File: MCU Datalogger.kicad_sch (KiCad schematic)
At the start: 18 parts, among them U1 24LC1025, U2 24LC1025, U3 DS1337S_, U4 ATMEGA328P-AU, Y1 Crystal, Y2 Crystal

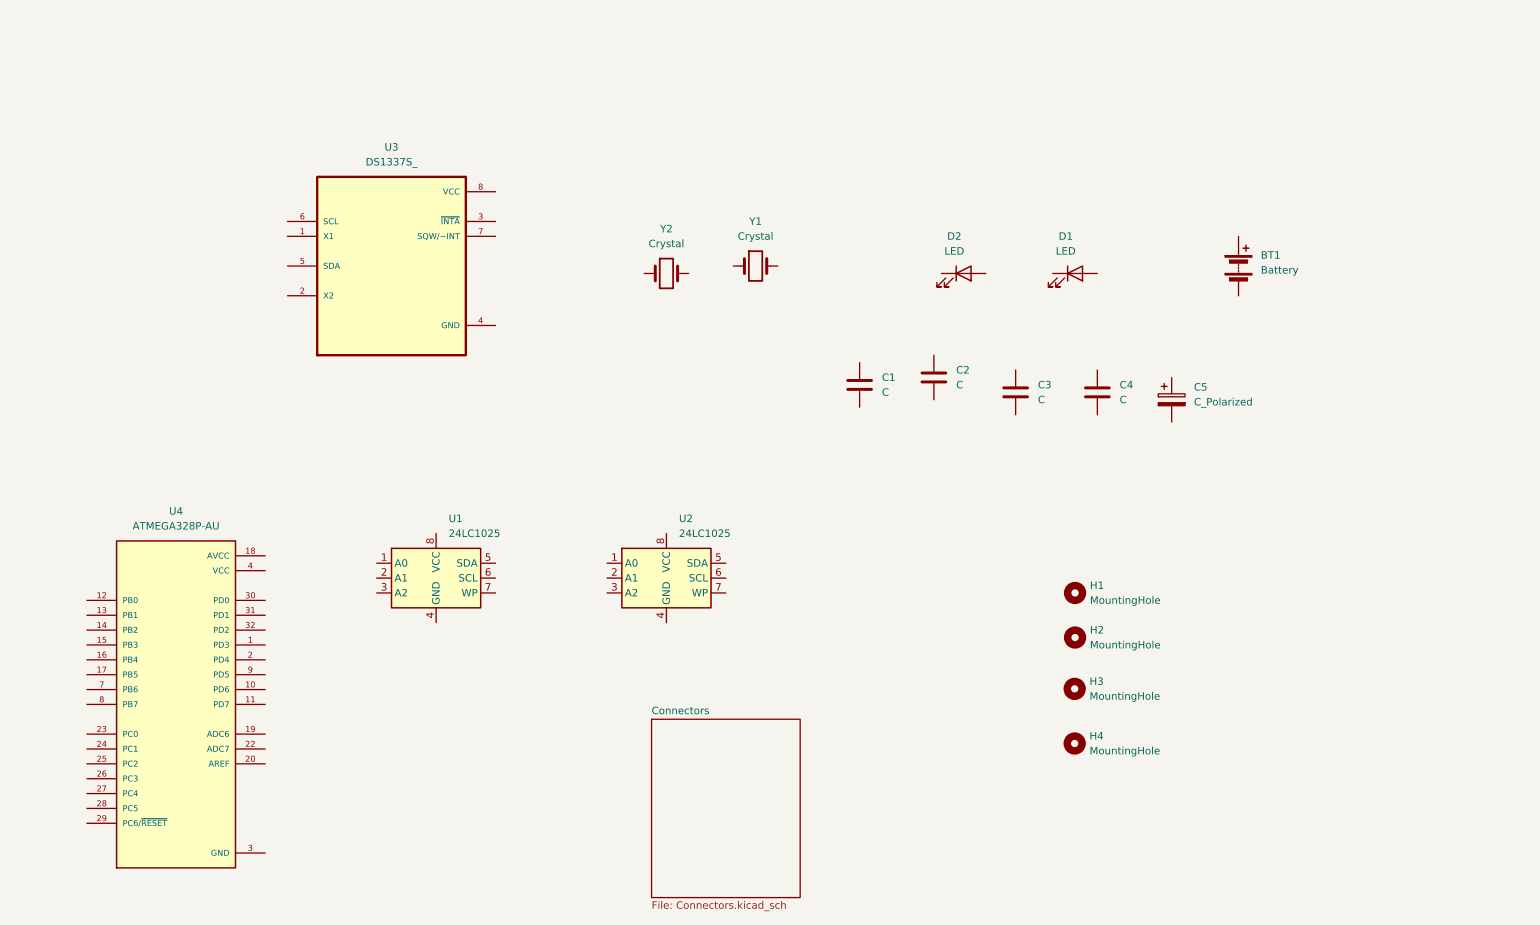
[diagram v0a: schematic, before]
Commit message: Changed location of symbols (arrange).
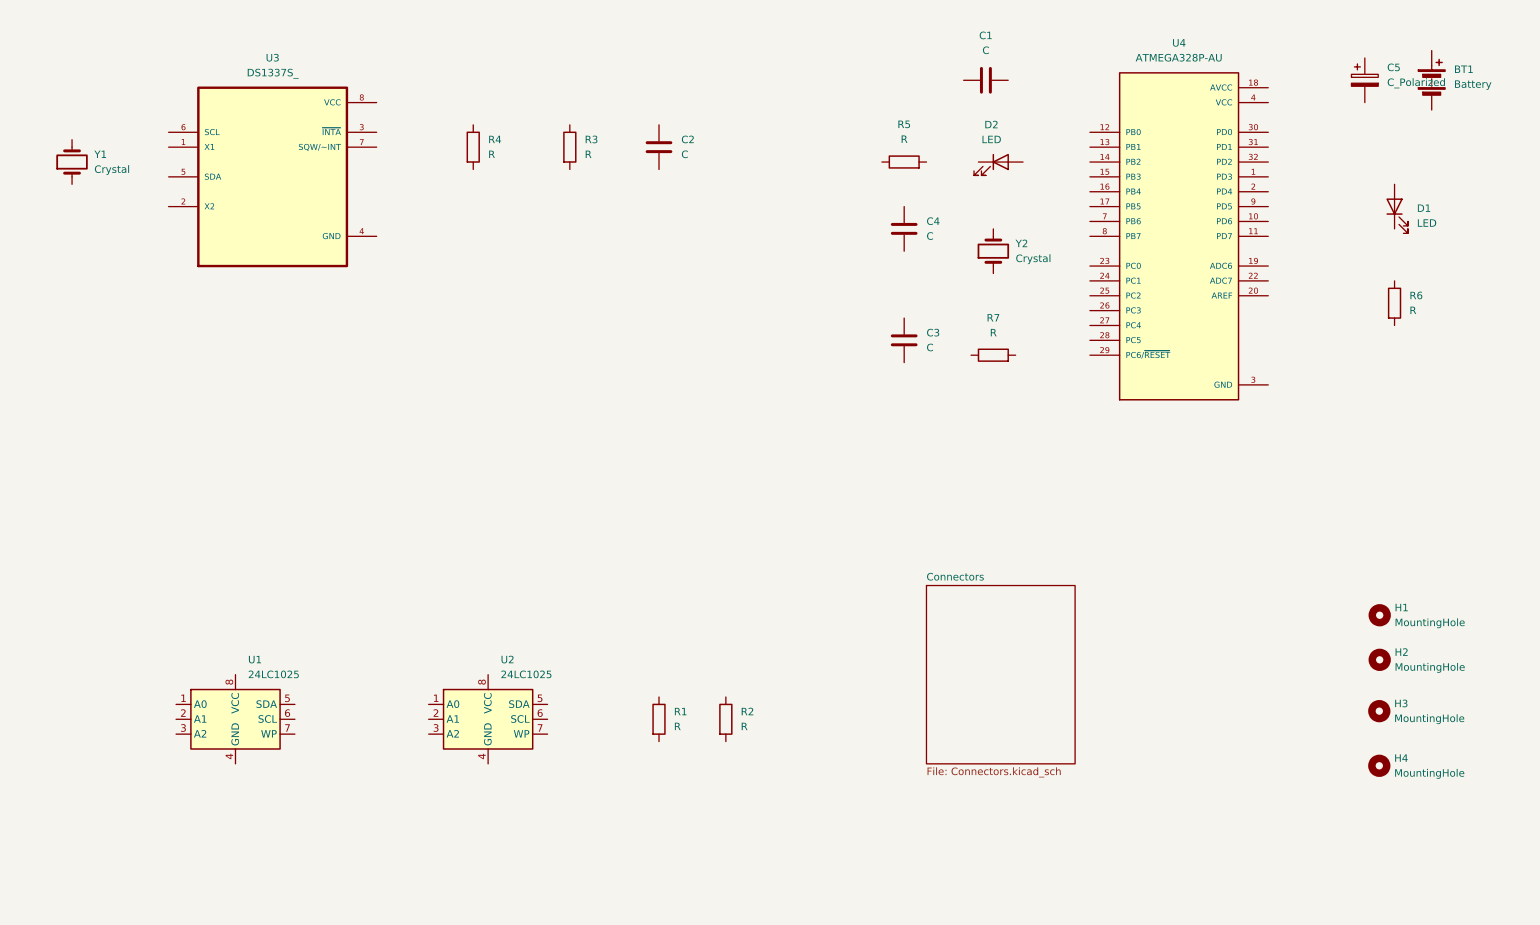
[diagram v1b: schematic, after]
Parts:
- added R1, R2, R3, R4, R5, R6, R7: R, symbol Device:R
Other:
- moved on the sheet: BT1, C1, C2, C3, C4, C5, D1, D2, H1, H2, H3, H4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

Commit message: edit component values
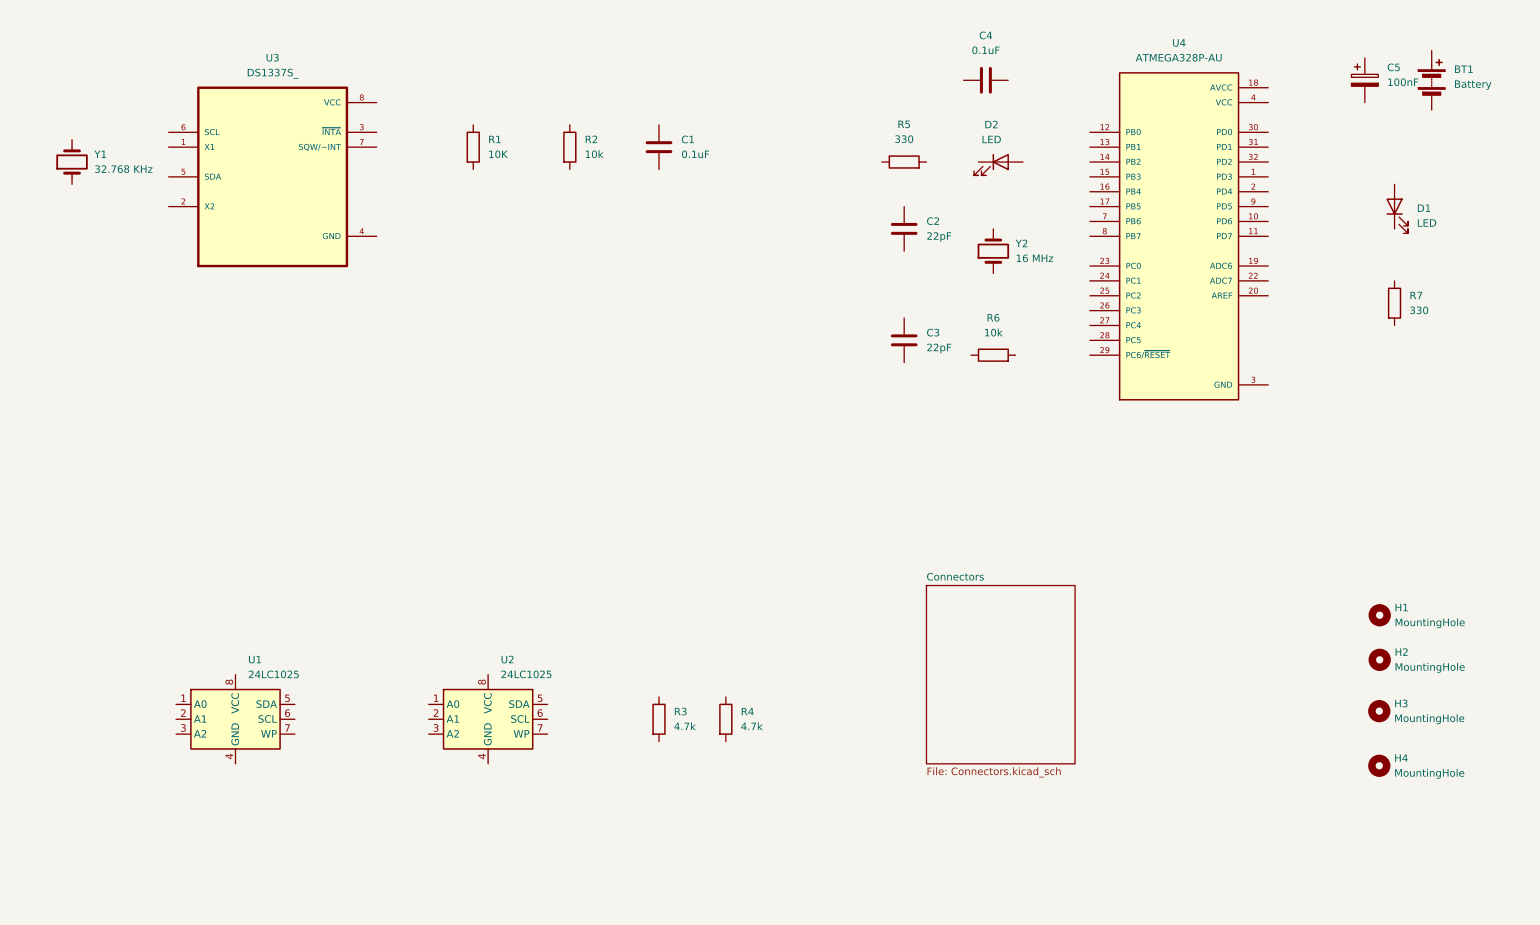
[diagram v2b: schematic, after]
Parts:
- C1: renamed from C2; value C -> 0.1uF
- C2: renamed from C4; value C -> 22pF
- C3: value C -> 22pF
- C4: renamed from C1; value C -> 0.1uF
- C5: value C_Polarized -> 100nF
- R1: renamed from R4; value R -> 10K
- R2: renamed from R3; value R -> 10k
- R3: renamed from R1; value R -> 4.7k
- R4: renamed from R2; value R -> 4.7k
- R5: value R -> 330
- R6: renamed from R7; value R -> 10k
- R7: renamed from R6; value R -> 330
- Y1: value Crystal -> 32.768 KHz
- Y2: value Crystal -> 16 MHz
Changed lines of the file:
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@@
 			)
 		)
-		(property "Value" "C"
+		(property "Value" "22pF"
 			(at 168.91 83.8199 0)
 			(effects
@@
 			)
 		)
+		(property "Purpose" ""
+			(at 165.1 82.55 0)
+			(effects
+				(font
+					(size 1.27 1.27)
+				)
+			)
+		)
 		(pin "1"
 		)
@@
 		(dnp no)
 		(fields_autoplaced yes)
-		(property "Reference" "R7"
+		(property "Reference" "R6"
 			(at 180.34 78.74 90)
 			(effects
@@
 			)
 		)
-		(property "Value" "R"
+		(property "Value" "10k"
 			(at 180.34 81.28 90)
 			(effects
@@
 			)
 		)
+		(property "Purpose" ""
+			(at 180.34 85.09 0)
+			(effects
+				(font
+					(size 1.27 1.27)
+				)
+			)
+		)
 		(pin "2"
 		)
@@
 			(project "MCU Datalogger"
 				(path "/b34ba724-37f1-4069-92d1-dfc9c20970e0"
-					(reference "R7")
+					(reference "R6")
 					(unit 1)
 				)
@@
 		(dnp no)
 		(fields_autoplaced yes)
-		(property "Reference" "C4"
+		(property "Reference" "C2"
 			(at 168.91 62.2299 0)
 			(effects
@@
 			)
 		)
-		(property "Value" "C"
+		(property "Value" "22pF"
 			(at 168.91 64.7699 0)
 			(effects
@@
 			)
 		)
+		(property "Purpose" ""
+			(at 165.1 63.5 0)
+			(effects
+				(font
+					(size 1.27 1.27)
+				)
+			)
+		)
 		(pin "1"
 		)
@@
 			(project "MCU Datalogger"
 				(path "/b34ba724-37f1-4069-92d1-dfc9c20970e0"
-					(reference "C4")
+					(reference "C2")
 					(unit 1)
 				)
@@
 		(dnp no)
 		(fields_autoplaced yes)
-		(property "Reference" "C2"
+		(property "Reference" "C1"
 			(at 127 48.2599 0)
 			(effects
@@
 			)
 		)
-		(property "Value" "C"
+		(property "Value" "0.1uF"
 			(at 127 50.7999 0)
 			(effects
@@
 			)
 		)
+		(property "Purpose" ""
+			(at 123.19 49.53 0)
+			(effects
+				(font
+					(size 1.27 1.27)
+				)
+			)
+		)
 		(pin "1"
 		)
@@
 			(project "MCU Datalogger"
 				(path "/b34ba724-37f1-4069-92d1-dfc9c20970e0"
-					(reference "C2")
+					(reference "C1")
 					(unit 1)
 				)
@@
 		(dnp no)
 		(fields_autoplaced yes)
-		(property "Reference" "R1"
+		(property "Reference" "R3"
 			(at 125.73 146.0499 0)
 			(effects
@@
 			)
 		)
-		(property "Value" "R"
+		(property "Value" "4.7k"
 			(at 125.73 148.5899 0)
 			(effects
@@
 			)
 		)
+		(property "Purpose" ""
+			(at 123.19 147.32 0)
+			(effects
+				(font
+					(size 1.27 1.27)
+				)
+			)
+		)
 		(pin "2"
 		)
@@
 			(project ""
 				(path "/b34ba724-37f1-4069-92d1-dfc9c20970e0"
-					(reference "R1")
+					(reference "R3")
 					(unit 1)
 				)
@@
 		(dnp no)
 		(fields_autoplaced yes)
-		(property "Reference" "R4"
+		(property "Reference" "R1"
 			(at 93.98 48.2599 0)
 			(effects
@@
 			)
 		)
-		(property "Value" "R"
+		(property "Value" "10K"
 			(at 93.98 50.7999 0)
 			(effects
@@
 			)
 		)
+		(property "Purpose" ""
+			(at 91.44 49.53 0)
+			(effects
+				(font
+					(size 1.27 1.27)
+				)
+			)
+		)
 		(pin "2"
 		)
@@
 			(project "MCU Datalogger"
 				(path "/b34ba724-37f1-4069-92d1-dfc9c20970e0"
-					(reference "R4")
+					(reference "R1")
 					(unit 1)
 				)
@@
 		(dnp no)
 		(fields_autoplaced yes)
-		(property "Reference" "C1"
+		(property "Reference" "C4"
 			(at 179.07 30.48 90)
 			(effects
@@
 			)
 		)
-		(property "Value" "C"
+		(property "Value" "0.1uF"
 			(at 179.07 33.02 90)
 			(effects
@@
 			)
 		)
+		(property "Purpose" ""
+			(at 179.07 38.1 0)
+			(effects
+				(font
+					(size 1.27 1.27)
+				)
+			)
+		)
 		(pin "1"
 		)
@@
 			(project ""
 				(path "/b34ba724-37f1-4069-92d1-dfc9c20970e0"
-					(reference "C1")
+					(reference "C4")
 					(unit 1)
 				)
@@
 		(dnp no)
 		(fields_autoplaced yes)
-		(property "Reference" "R3"
+		(property "Reference" "R2"
 			(at 110.49 48.2599 0)
 			(effects
@@
 			)
 		)
-		(property "Value" "R"
+		(property "Value" "10k"
 			(at 110.49 50.7999 0)
 			(effects
@@
 			)
 		)
+		(property "Purpose" ""
+			(at 107.95 49.53 0)
+			(effects
+				(font
+					(size 1.27 1.27)
+				)
+			)
+		)
 		(pin "2"
 		)
@@
 			(project "MCU Datalogger"
 				(path "/b34ba724-37f1-4069-92d1-dfc9c20970e0"
-					(reference "R3")
+					(reference "R2")
 					(unit 1)
 				)
@@
 		(dnp no)
 		(fields_autoplaced yes)
-		(property "Reference" "R2"
+		(property "Reference" "R4"
 			(at 137.16 146.0499 0)
 			(effects
@@
 			)
 		)
-		(property "Value" "R"
+		(property "Value" "4.7k"
 			(at 137.16 148.5899 0)
 			(effects
@@
 			)
 		)
+		(property "Purpose" ""
+			(at 134.62 147.32 0)
+			(effects
+				(font
+					(size 1.27 1.27)
+				)
+			)
+		)
 		(pin "2"
 		)
@@
 			(project "MCU Datalogger"
 				(path "/b34ba724-37f1-4069-92d1-dfc9c20970e0"
-					(reference "R2")
+					(reference "R4")
 					(unit 1)
 				)
@@
 		(on_board yes)
 		(dnp no)
-		(property "Reference" "R6"
+		(property "Reference" "R7"
 			(at 251.46 74.9299 0)
 			(effects
@@
 			)
 		)
-		(property "Value" "R"
+		(property "Value" "330"
 			(at 251.46 77.4699 0)
 			(effects
@@
 			)
 		)
+		(property "Purpose" ""
+			(at 248.92 76.2 0)
+			(effects
+				(font
+					(size 1.27 1.27)
+				)
+			)
+		)
 		(pin "2"
 		)
@@
 			(project "MCU Datalogger"
 				(path "/b34ba724-37f1-4069-92d1-dfc9c20970e0"
-					(reference "R6")
+					(reference "R7")
 					(unit 1)
 				)
@@
 			)
 		)
-		(property "Value" "Crystal"
+		(property "Value" "16 MHz"
 			(at 184.15 68.5799 90)
 			(effects
@@
 			)
 		)
+		(property "Purpose" ""
+			(at 180.34 67.31 0)
+			(effects
+				(font
+					(size 1.27 1.27)
+				)
+			)
+		)
 		(pin "2"
 		)
@@
 			)
 		)
-		(property "Value" "Crystal"
+		(property "Value" "32.768 KHz"
 			(at 26.67 53.3399 90)
 			(effects
@@
 			)
 		)
+		(property "Purpose" ""
+			(at 22.86 52.07 0)
+			(effects
+				(font
+					(size 1.27 1.27)
+				)
+			)
+		)
 		(pin "2"
 		)
@@
 			)
 		)
-		(property "Value" "R"
+		(property "Value" "330"
 			(at 165.1 48.2092 90)
 			(effects
@@
 			)
 		)
+		(property "Purpose" ""
+			(at 165.1 52.07 0)
+			(effects
+				(font
+					(size 1.27 1.27)
+				)
+			)
+		)
 		(pin "2"
 		)
@@
 			)
 		)
-		(property "Value" "C_Polarized"
+		(property "Value" "100nF"
 			(at 247.65 38.4809 0)
 			(effects
@@
 			)
 		)
+		(property "Purpose" ""
+			(at 243.84 38.1 0)
+			(effects
+				(font
+					(size 1.27 1.27)
+				)
+			)
+		)

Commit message: completed symbol-footprint assiciations
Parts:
- BT1: footprint (none) -> Connector_PinHeader_2.54mm:PinHeader_1x02_P2.54mm_Vertical
- C1, C2, C3, C4, C5: footprint (none) -> Capacitor_SMD:C_0805_2012Metric
- D1, D2: footprint (none) -> LED_SMD:LED_0805_2012Metric
- H1, H2, H3, H4: footprint (none) -> MountingHole:MountingHole_2.1mm
- R1, R2, R3, R4, R5, R6, R7: footprint (none) -> Resistor_SMD:R_0805_2012Metric
- U1, U2: footprint (none) -> Package_SO:SOIC-8_5.3x5.3mm_P1.27mm
- U3: footprint DS1337S_:SOIC127P600X175-8N -> footprints:SOIC127P600X175-8N
- U4: footprint ATMEGA328P-AU:QFP80P900X900X120-32N -> footprints:QFP80P900X900X120-32N
- Y1, Y2: footprint (none) -> Crystal:Crystal_SMD_5032-2Pin_5.0x3.2mm
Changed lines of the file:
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@@
 			)
 		)
-		(property "Footprint" "DS1337S_:SOIC127P600X175-8N"
+		(property "Footprint" "footprints:SOIC127P600X175-8N"
 			(at 57.15 54.61 0)
 			(effects
@@
 			)
 		)
-		(property "Footprint" ""
+		(property "Footprint" "Capacitor_SMD:C_0805_2012Metric"
 			(at 166.0652 86.36 0)
 			(effects
@@
 			)
 		)
-		(property "Footprint" ""
+		(property "Footprint" "Package_SO:SOIC-8_5.3x5.3mm_P1.27mm"
 			(at 50.8 147.32 0)
 			(effects
@@
 			)
 		)
-		(property "Footprint" ""
+		(property "Footprint" "Resistor_SMD:R_0805_2012Metric"
 			(at 180.34 86.868 90)
 			(effects
@@
 			)
 		)
-		(property "Footprint" ""
+		(property "Footprint" "LED_SMD:LED_0805_2012Metric"
 			(at 248.92 59.69 0)
 			(effects
@@
 			)
 		)
-		(property "Footprint" ""
+		(property "Footprint" "Connector_PinHeader_2.54mm:PinHeader_1x02_P2.54mm_Vertical"
 			(at 255.27 36.576 90)
 			(effects
@@
 			)
 		)
-		(property "Footprint" ""
+		(property "Footprint" "Capacitor_SMD:C_0805_2012Metric"
 			(at 166.0652 67.31 0)
 			(effects
@@
 			)
 		)
-		(property "Footprint" ""
+		(property "Footprint" "Package_SO:SOIC-8_5.3x5.3mm_P1.27mm"
 			(at 93.98 147.32 0)
 			(effects
@@
 			)
 		)
-		(property "Footprint" ""
+		(property "Footprint" "Capacitor_SMD:C_0805_2012Metric"
 			(at 124.1552 53.34 0)
 			(effects
@@
 			)
 		)
-		(property "Footprint" ""
+		(property "Footprint" "Resistor_SMD:R_0805_2012Metric"
 			(at 121.412 147.32 90)
 			(effects
@@
 			)
 		)
-		(property "Footprint" ""
+		(property "Footprint" "Resistor_SMD:R_0805_2012Metric"
 			(at 89.662 49.53 90)
 			(effects
@@
 			)
 		)
-		(property "Footprint" ""
+		(property "Footprint" "MountingHole:MountingHole_2.1mm"
 			(at 246.38 137.16 0)
 			(effects
@@
 			)
 		)
-		(property "Footprint" ""
+		(property "Footprint" "Capacitor_SMD:C_0805_2012Metric"
 			(at 182.88 37.1348 0)
 			(effects
@@
 			)
 		)
-		(property "Footprint" ""
+		(property "Footprint" "MountingHole:MountingHole_2.1mm"
 			(at 246.3121 155.273 0)
 			(effects
@@
 			)
 		)
-		(property "Footprint" ""
+		(property "Footprint" "Resistor_SMD:R_0805_2012Metric"
 			(at 106.172 49.53 90)
 			(effects
@@
 			)
 		)
-		(property "Footprint" ""
+		(property "Footprint" "Resistor_SMD:R_0805_2012Metric"
 			(at 132.842 147.32 90)
 			(effects
@@
 			)
 		)
-		(property "Footprint" ""
+		(property "Footprint" "MountingHole:MountingHole_2.1mm"
 			(at 246.3121 145.9332 0)
 			(effects
@@
 			)
 		)
-		(property "Footprint" ""
+		(property "Footprint" "LED_SMD:LED_0805_2012Metric"
 			(at 181.61 52.07 0)
 			(effects
@@
 			)
 		)
-		(property "Footprint" ""
+		(property "Footprint" "Resistor_SMD:R_0805_2012Metric"
 			(at 247.142 76.2 90)
 			(effects
@@
 			)
 		)
-		(property "Footprint" ""
+		(property "Footprint" "MountingHole:MountingHole_2.1mm"
 			(at 246.38 129.54 0)
 			(effects
@@
 			)
 		)
-		(property "Footprint" ""
+		(property "Footprint" "Crystal:Crystal_SMD_5032-2Pin_5.0x3.2mm"
 			(at 180.34 67.31 0)
 			(effects
@@
 			)
 		)
-		(property "Footprint" "ATMEGA328P-AU:QFP80P900X900X120-32N"
+		(property "Footprint" "footprints:QFP80P900X900X120-32N"
 			(at 212.09 64.77 0)
 			(effects
@@
 			)
 		)
-		(property "Footprint" ""
+		(property "Footprint" "Crystal:Crystal_SMD_5032-2Pin_5.0x3.2mm"
 			(at 22.86 52.07 0)
 			(effects
@@
 			)
 		)
-		(property "Footprint" ""
+		(property "Footprint" "Resistor_SMD:R_0805_2012Metric"
 			(at 165.1 53.848 90)
 			(effects
@@
 			)
 		)
-		(property "Footprint" ""
+		(property "Footprint" "Capacitor_SMD:C_0805_2012Metric"
 			(at 244.8052 41.91 0)
 			(effects
